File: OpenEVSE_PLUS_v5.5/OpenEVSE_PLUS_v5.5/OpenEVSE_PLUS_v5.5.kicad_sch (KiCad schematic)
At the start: 75 parts, among them IC1 HCPL-2731, IC2 MEGA8-AI, IC3 LMV358, IC4 LMV358, IC5 AQH1213, IC6 TC1044S, Q1 16000, Q2 BCX70SMD, Q3 BCX70SMD

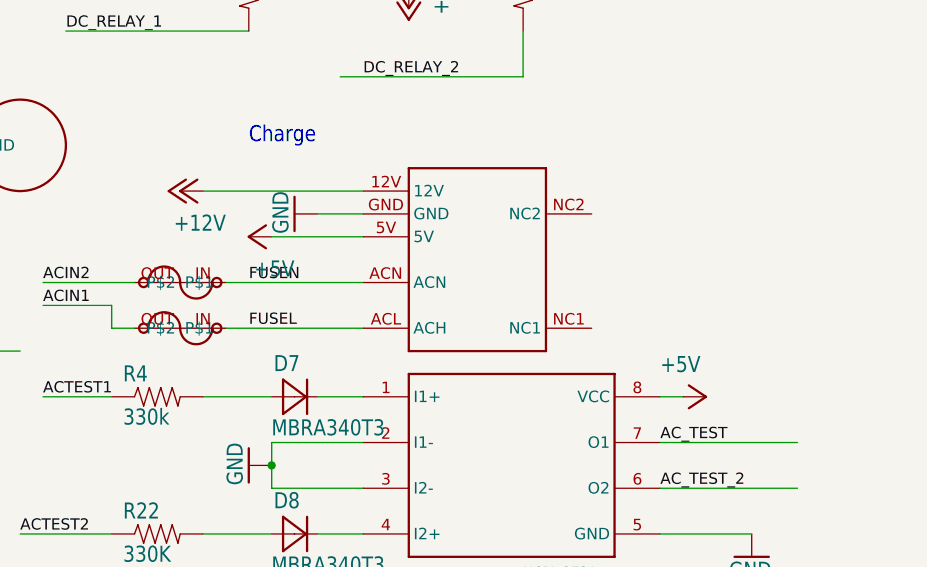
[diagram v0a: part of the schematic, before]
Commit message: WIP new power module TMLM 04225
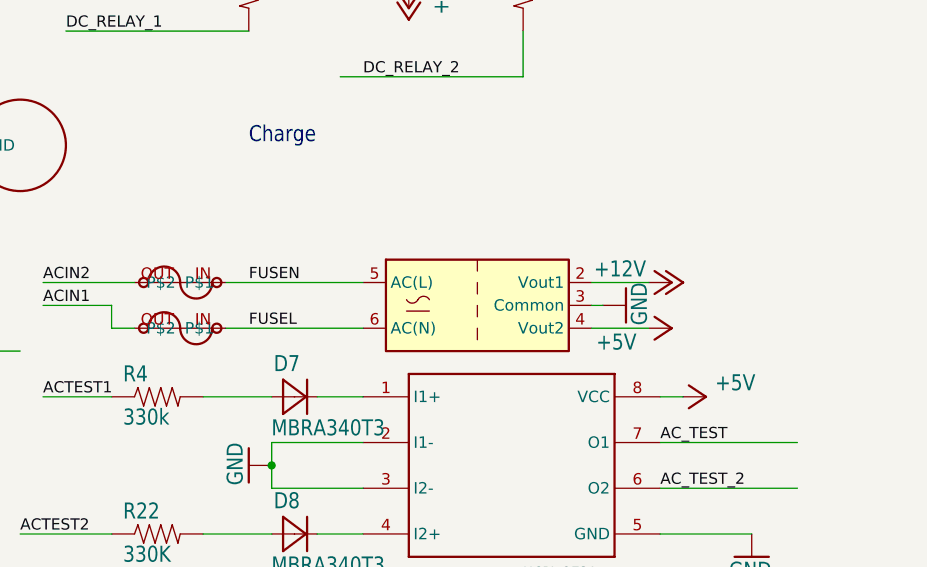
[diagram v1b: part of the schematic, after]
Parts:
- PS1: footprint OpenEVSE_PLUS_v5.5:MPM-04E-1205 -> Converter_ACDC:Converter_ACDC_TRACO_TMLM-04_THT; symbol OpenEVSE_PLUS_v5.5-eagle-import:MPM-04E-1205 -> Converter_ACDC:TMLM04225
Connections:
- net +12V: now also PS1.2 (Vout1); no longer PS1.12V
- net +5V: now also PS1.4 (Vout2); no longer PS1.5V
- net FUSEL: now also PS1.6 (AC(N)); no longer PS1.ACL (ACH)
- net FUSEN: now also PS1.5 (AC(L)); no longer PS1.ACN
- net GND: now also PS1.3 (Common); no longer PS1.GND
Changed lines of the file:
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@@
 	(wire
 		(pts
-			(xy 218.44 160.02) (xy 228.6 160.02)
-		)
-		(stroke
-			(width 0.1524)
-			(type solid)
-		)
-	)
-	(wire
-		(pts
 			(xy 195.58 78.74) (xy 187.96 78.74)
 		)
@@
 		)
 	)
+	(wire
+		(pts
+			(xy 254 170.18) (xy 260.35 170.18)
+		)
+		(stroke
+			(width 0)
+			(type default)
+		)
+	)
 	(polyline
 		(pts
@@
 	(wire
 		(pts
+			(xy 254 165.1) (xy 260.35 165.1)
+		)
+		(stroke
+			(width 0)
+			(type default)
+		)
+	)
+	(wire
+		(pts
 			(xy 254 223.52) (xy 266.7 223.52)
 		)
@@
 	(wire
 		(pts
-			(xy 210.82 154.94) (xy 228.6 154.94)
-		)
-		(stroke
-			(width 0.1524)
-			(type solid)
-		)
-	)
-	(wire
-		(pts
 			(xy 195.58 53.34) (xy 195.58 78.74)
 		)
@@
 	(wire
 		(pts
+			(xy 254 167.64) (xy 255.27 167.64)
+		)
+		(stroke
+			(width 0)
+			(type default)
+		)
+	)
+	(wire
+		(pts
 			(xy 99.06 68.58) (xy 99.06 71.12)
 		)
@@
 	(wire
 		(pts
-			(xy 228.6 157.48) (xy 223.52 157.48)
-		)
-		(stroke
-			(width 0.1524)
-			(type solid)
-		)
-	)
-	(wire
-		(pts
 			(xy 111.76 91.44) (xy 121.92 91.44)
 		)
@@
 	(symbol
 		(lib_id "OpenEVSE_PLUS_v5.5-eagle-import:+5V")
-		(at 215.9 160.02 90)
+		(at 262.89 170.18 270)
+		(mirror x)
 		(unit 1)
 		(exclude_from_sim no)
@@
 		(dnp no)
 		(property "Reference" "#P+1"
-			(at 215.9 160.02 0)
+			(at 262.89 170.18 0)
 			(effects
 				(font
@@
 		)
 		(property "Value" "+5V"
-			(at 220.98 162.56 90)
+			(at 254.508 170.688 90)
 			(effects
 				(font
@@
 		)
 		(property "Footprint" ""
-			(at 215.9 160.02 0)
+			(at 262.89 170.18 0)
 			(effects
 				(font
@@
 		)
 		(property "Datasheet" ""
-			(at 215.9 160.02 0)
+			(at 262.89 170.18 0)
 			(effects
 				(font
@@
 		)
 		(property "Description" ""
-			(at 215.9 160.02 0)
+			(at 262.89 170.18 0)
 			(effects
 				(font
@@
 	)
 	(symbol
-		(lib_id "OpenEVSE_PLUS_v5.5-eagle-import:MPM-04E-1205")
-		(at 246.38 160.02 0)
+		(lib_id "Converter_ACDC:TMLM04225")
+		(at 241.3 167.64 0)
 		(unit 1)
 		(exclude_from_sim no)
@@
 		(dnp no)
 		(property "Reference" "PS1"
-			(at 246.38 160.02 0)
+			(at 241.3 167.64 0)
 			(effects
 				(font
@@
 		)
 		(property "Value" "MPM-04E-1205"
-			(at 246.38 160.02 0)
+			(at 241.3 167.64 0)
 			(effects
 				(font
@@
 			)
 		)
-		(property "Footprint" "OpenEVSE_PLUS_v5.5:MPM-04E-1205"
-			(at 246.38 160.02 0)
+		(property "Footprint" "Converter_ACDC:Converter_ACDC_TRACO_TMLM-04_THT"
+			(at 241.3 176.53 0)
 			(effects
 				(font
@@
 			)
 		)
-		(property "Datasheet" ""
-			(at 246.38 160.02 0)
+		(property "Datasheet" "https://www.tracopower.com/products/tmlm.pdf"
+			(at 241.3 167.64 0)
 			(effects
 				(font
@@
 			)
 		)
-		(property "Description" ""
-			(at 246.38 160.02 0)
+		(property "Description" "12V 250mA / 5V 120mA AC/DC dual output, low noise power module"
+			(at 241.3 167.64 0)
 			(effects
 				(font
@@
 			)
 		)
-		(pin "12V"
-		)
-		(pin "5V"
-		)
-		(pin "ACL"
+		(pin "6"
 		)
-		(pin "ACN"
+		(pin "5"
 		)
-		(pin "GND"
+		(pin "2"
 		)
-		(pin "NC1"
+		(pin "3"
 		)
-		(pin "NC2"
+		(pin "4"
 		)
 		(instances
@@
 		)
 		(property "Value" "+5V"
-			(at 261.62 175.26 90)
+			(at 267.716 177.292 90)
 			(effects
 				(font
@@
 	(symbol
 		(lib_id "OpenEVSE_PLUS_v5.5-eagle-import:+12V")
-		(at 208.28 154.94 90)
+		(at 262.89 165.1 270)
+		(mirror x)
 		(unit 1)
 		(exclude_from_sim no)
@@
 		(dnp no)
 		(property "Reference" "#P+9"
-			(at 208.28 154.94 0)
+			(at 262.89 165.1 0)
 			(effects
 				(font
@@
 		)
 		(property "Value" "+12V"
-			(at 213.36 157.48 90)
+			(at 254.254 162.56 90)
 			(effects
 				(font
@@
 		)
 		(property "Footprint" ""
-			(at 208.28 154.94 0)
+			(at 262.89 165.1 0)
 			(effects
 				(font
@@
 		)
 		(property "Datasheet" ""
-			(at 208.28 154.94 0)
+			(at 262.89 165.1 0)
 			(effects
 				(font
@@
 		)
 		(property "Description" ""
-			(at 208.28 154.94 0)
+			(at 262.89 165.1 0)
 			(effects
 				(font
@@
 	(symbol
 		(lib_id "OpenEVSE_PLUS_v5.5-eagle-import:GND")
-		(at 220.98 157.48 270)
+		(at 257.81 167.64 90)
+		(mirror x)
 		(unit 1)
 		(exclude_from_sim no)
@@
 		(dnp no)
 		(property "Reference" "#GND2"
-			(at 220.98 157.48 0)
+			(at 257.81 167.64 0)
 			(effects
 				(font
@@
 		)
 		(property "Value" "GND"
-			(at 218.44 154.94 0)
+			(at 260.35 165.1 0)
 			(effects
 				(font
@@
 		)
 		(property "Footprint" ""
-			(at 220.98 157.48 0)
+			(at 257.81 167.64 0)
 			(effects
 				(font
@@
 		)
 		(property "Datasheet" ""
-			(at 220.98 157.48 0)
+			(at 257.81 167.64 0)
 			(effects
 				(font
@@
 		)
 		(property "Description" ""
-			(at 220.98 157.48 0)
+			(at 257.81 167.64 0)
 			(effects
 				(font
